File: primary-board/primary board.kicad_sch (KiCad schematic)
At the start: 30 parts, among them J1 USB_C, J10 Motor Connector Right, J2 Sensor_Forward, J3 Sensor_Right, J4 Sensor_Left, J5 I2C Breakout, J9 Motor Connector Left, SW1 SW_SPST, SW2 SW_SPST, U1 ESP32-S3-1, U5 DRV8411ARTER

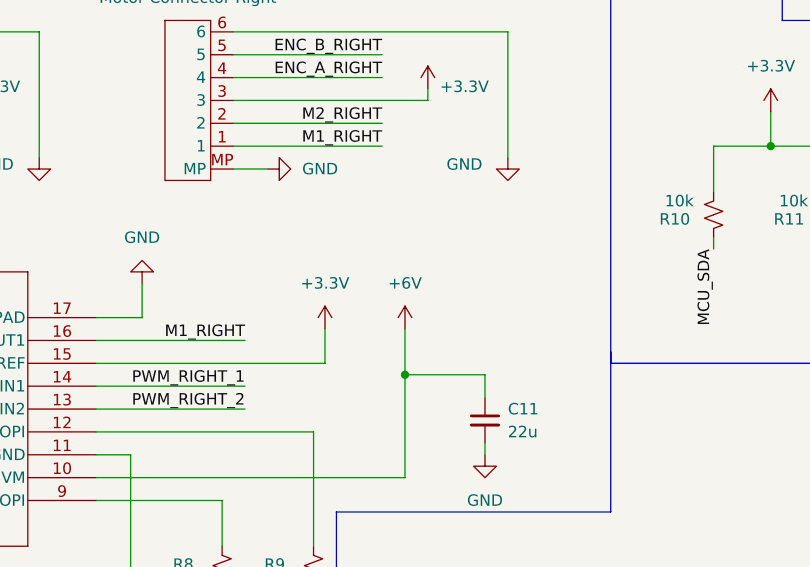
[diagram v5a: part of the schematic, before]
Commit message: scrapped flawed power path, using a switch instead
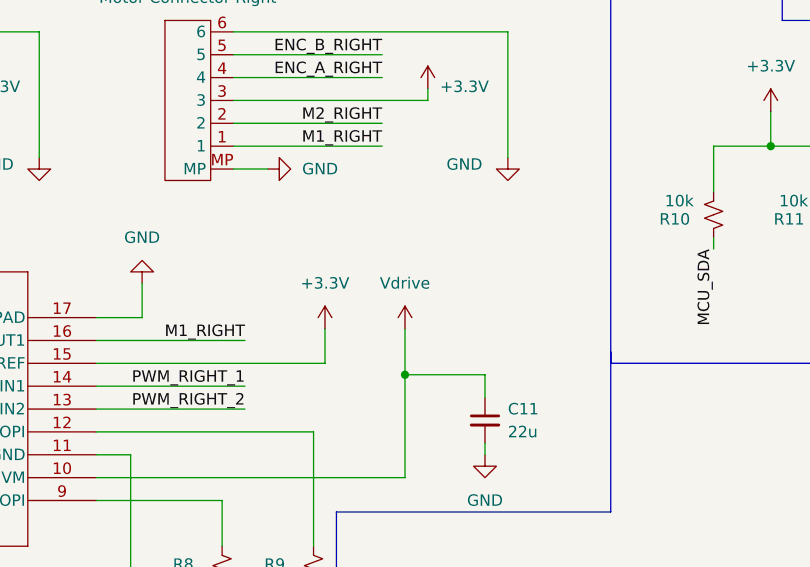
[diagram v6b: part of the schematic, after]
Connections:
- net +6V renamed Vdrive
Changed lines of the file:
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@@
-	)
-	(symbol
-		(lib_id "power:+6V")
-		(at 182.88 144.78 0)
-		(unit 1)
-		(exclude_from_sim no)
-		(in_bom yes)
-		(on_board yes)
-		(dnp no)
-		(fields_autoplaced yes)
-		(property "Reference" "#PWR031"
-			(at 182.88 148.59 0)
-			(effects
-				(font
-					(size 1.27 1.27)
-				)
-				(hide yes)
-			)
-		)
-		(property "Value" "+6V"
-			(at 182.88 139.7 0)
-			(effects
-				(font
-					(size 1.27 1.27)
-				)
-			)
-		)
-		(property "Footprint" ""
-			(at 182.88 144.78 0)
-			(effects
-				(font
-					(size 1.27 1.27)
-				)
-				(hide yes)
-			)
-		)
-		(property "Datasheet" ""
-			(at 182.88 144.78 0)
-			(effects
-				(font
-					(size 1.27 1.27)
-				)
-				(hide yes)
-			)
-		)
-		(property "Description" "Power symbol creates a global label with name \"+6V\""
-			(at 182.88 144.78 0)
-			(effects
-				(font
-					(size 1.27 1.27)
-				)
-				(hide yes)
-			)
-		)
-		(pin "1"
-		)
-		(instances
-			(project ""
-				(path "/e926887c-cd26-4f47-be51-3352b14f6743"
-					(reference "#PWR031")
-					(unit 1)
-				)
-			)
-		)
 	)
 	(symbol
@@
 					(unit 1)
 				)
+			)
+		)
+	)
+	(symbol
+		(lib_id "power:Vdrive")
+		(at 182.88 144.78 0)
+		(unit 1)
+		(exclude_from_sim no)
+		(in_bom yes)
+		(on_board yes)
+		(dnp no)
+		(fields_autoplaced yes)
+		(property "Reference" "#PWR041"
+			(at 182.88 148.59 0)
+			(effects
+				(font
+					(size 1.27 1.27)
+				)
+				(hide yes)
+			)
+		)
+		(property "Value" "Vdrive"
+			(at 182.88 139.7 0)
+			(effects
+				(font
+					(size 1.27 1.27)
+				)
+			)
+		)
+		(property "Footprint" ""
+			(at 182.88 144.78 0)
+			(effects
+				(font
+					(size 1.27 1.27)
+				)
+				(hide yes)
+			)
+		)
+		(property "Datasheet" ""
+			(at 182.88 144.78 0)
+			(effects
+				(font
+					(size 1.27 1.27)
+				)
+				(hide yes)
+			)
+		)
+		(property "Description" "Power symbol creates a global label with name \"Vdrive\""
+			(at 182.88 144.78 0)
+			(effects
+				(font
+					(size 1.27 1.27)
+				)
+				(hide yes)
+			)
+		)
+		(pin "1"
+		)
+		(instances
+			(project ""
+				(path "/e926887c-cd26-4f47-be51-3352b14f6743"
+					(reference "#PWR041")
+					(unit 1)
+				)

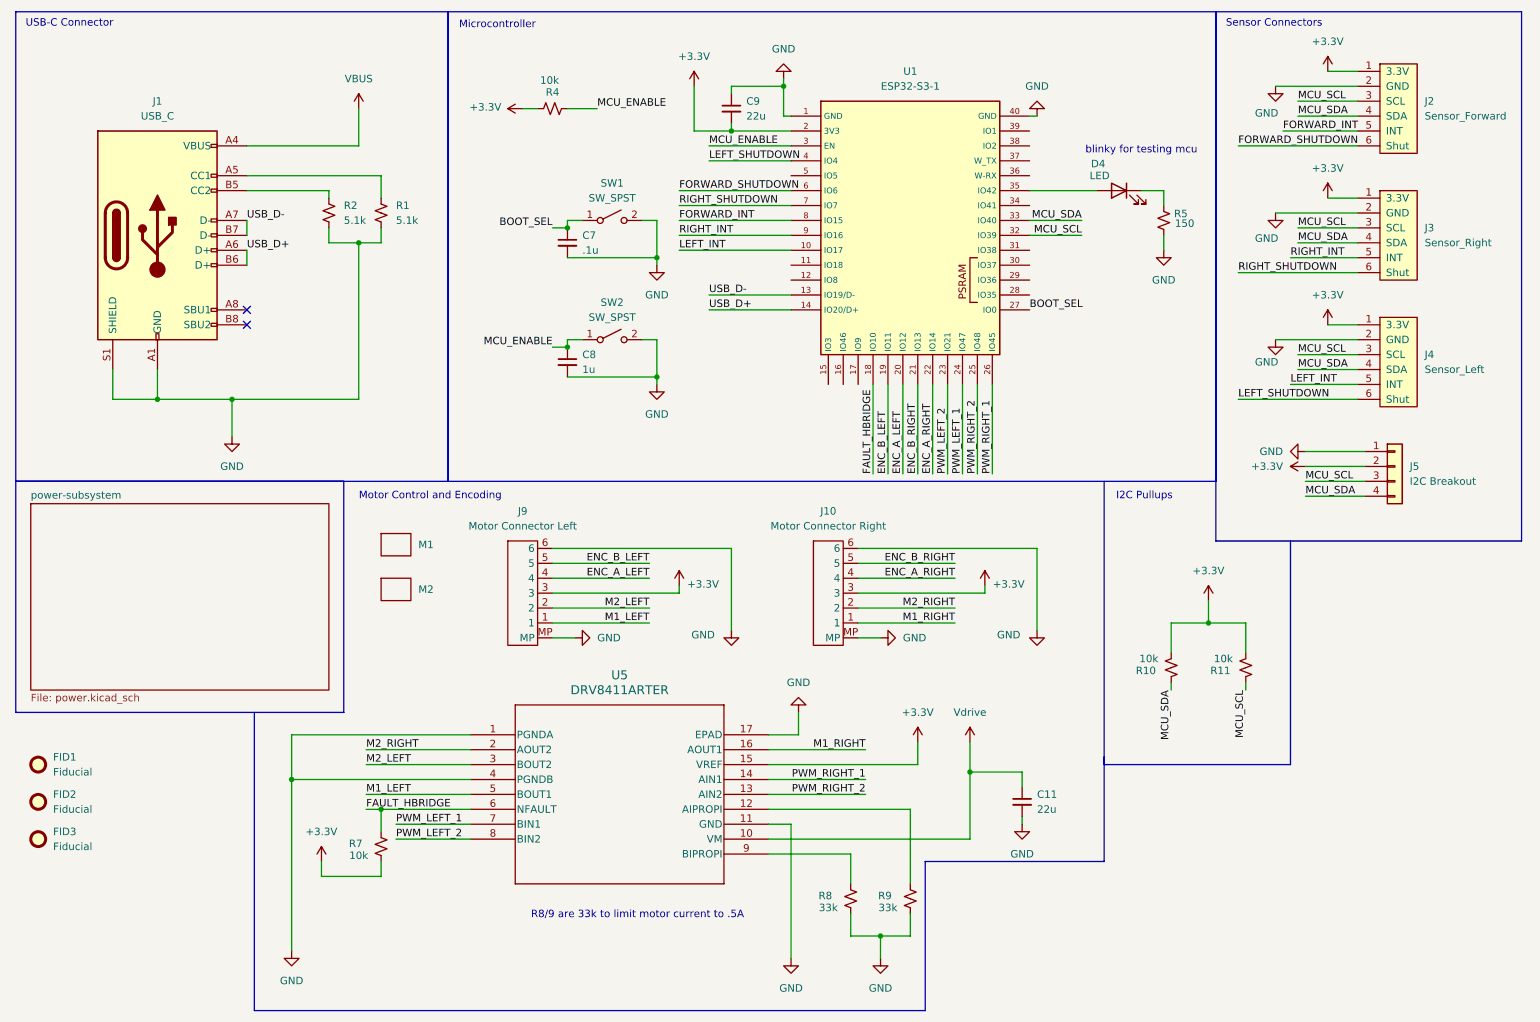
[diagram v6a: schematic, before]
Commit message: removed digital sensors
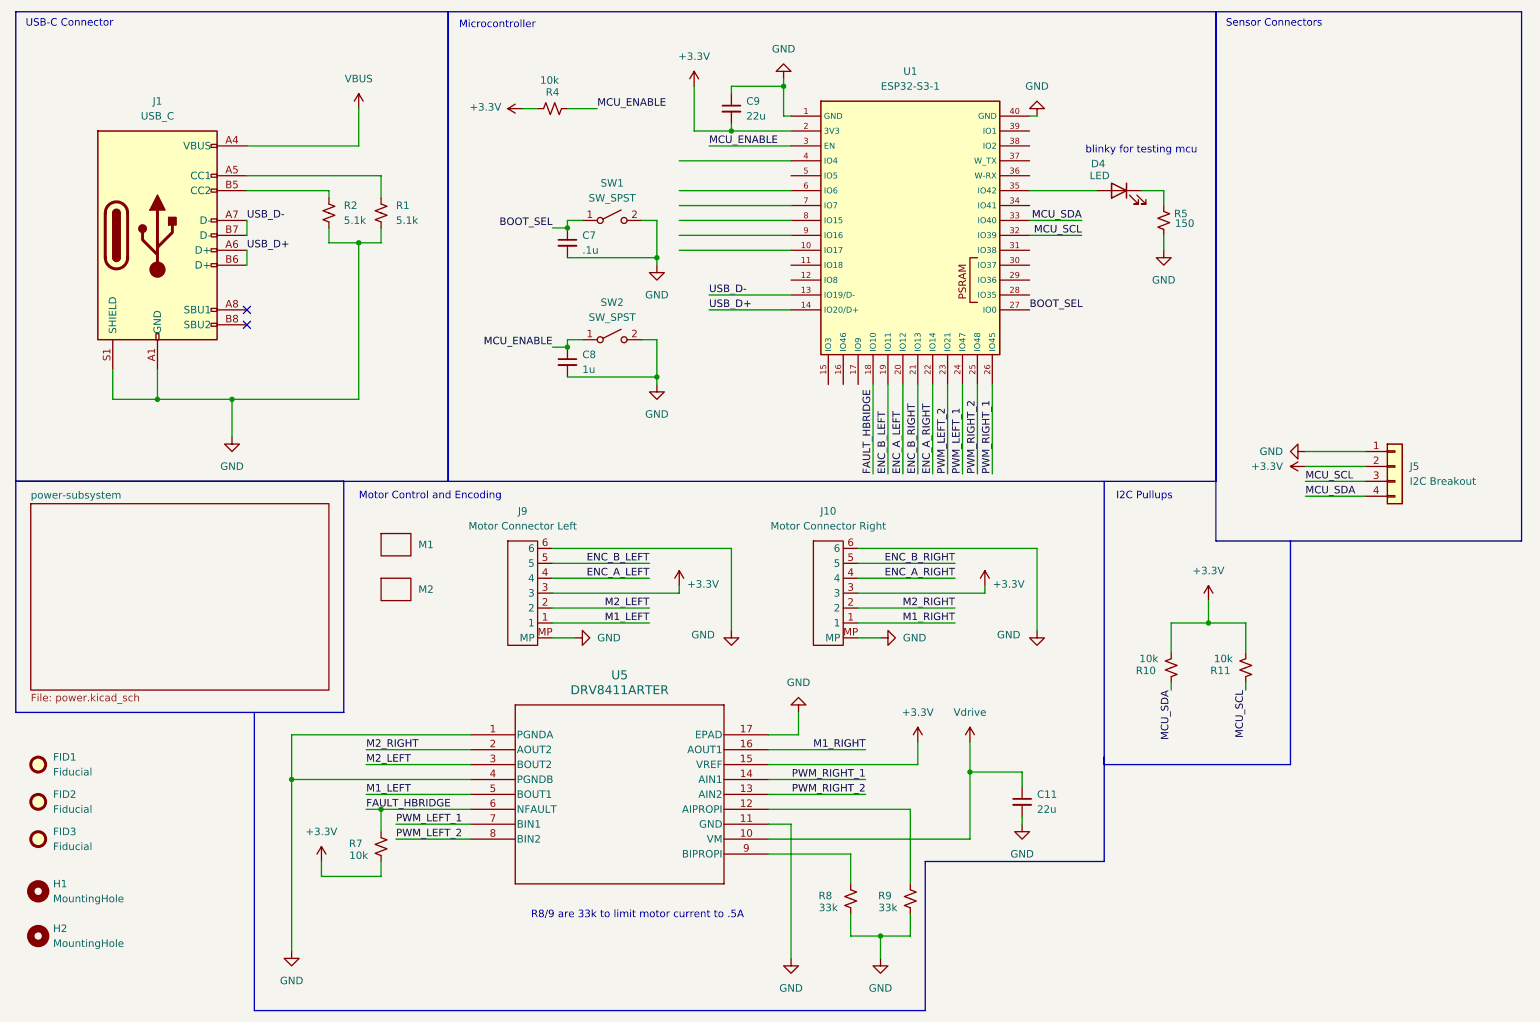
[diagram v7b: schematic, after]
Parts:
- removed J2: Sensor_Forward, Connector_PinSocket_2.54mm:PinSocket_1x06_P2.54mm_Vertical, symbol mouseLib:TofF breakout
- removed J3: Sensor_Right, Connector_PinSocket_2.54mm:PinSocket_1x06_P2.54mm_Vertical, symbol mouseLib:TofF breakout
- removed J4: Sensor_Left, Connector_PinSocket_2.54mm:PinSocket_1x06_P2.54mm_Vertical, symbol mouseLib:TofF breakout
- added H1, H2: MountingHole, MountingHole:MountingHole_2.2mm_M2, symbol Mechanical:MountingHole
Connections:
- net FORWARD_INT: no longer names the net of U1.8 (IO15)
- net FORWARD_SHUTDOWN: no longer names the net of U1.6 (IO6)
- net LEFT_INT: no longer names the net of U1.10 (IO17)
- net LEFT_SHUTDOWN: no longer names the net of U1.4 (IO4)
- net RIGHT_INT: no longer names the net of U1.9 (IO16)
- net RIGHT_SHUTDOWN: no longer names the net of U1.7 (IO7)

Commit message: analog work
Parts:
- removed J5: I2C Breakout, Connector_PinSocket_2.54mm:PinSocket_1x04_P2.54mm_Vertical, symbol Connector_Generic:Conn_01x04
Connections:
- net ir_led_front_right: now reaches U1.10 (IO17)
- net ir_led_front_left: now reaches U1.15 (IO3)
- net ir_led_left: now reaches U1.17 (IO9)
- net analog_sense_left: now reaches U1.4 (IO4)
- net analog_sense_front_left: now reaches U1.5 (IO5)
- net analog_sense_front_right: now reaches U1.6 (IO6)
- net analog_sense_right: now reaches U1.7 (IO7)
- net ir_led_right: now reaches U1.9 (IO16)
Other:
- added sheet sensors (sensors.kicad_sch)
- moved on the sheet: C7, C8, SW1, SW2
